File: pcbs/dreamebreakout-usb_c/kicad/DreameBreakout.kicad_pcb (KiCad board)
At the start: 2 copper layers, 18 x 61.5 mm, 10 parts, among them J1 SoC Breakout, J1.1 To Robot SoC, J1.2 To Robot MCU, J2 MCU Breakout, J3 OTG_USB, SW1 SoC_Boot_SEL_BTN

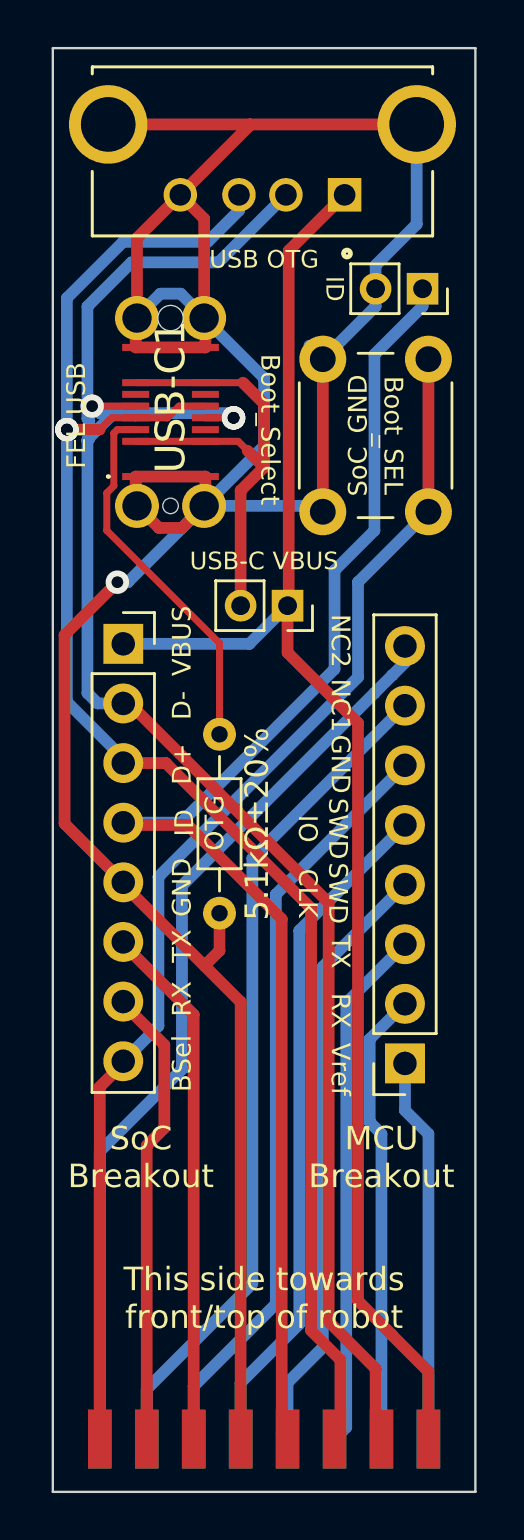
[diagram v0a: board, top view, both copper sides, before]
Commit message: Replaced micro-USB with USB-C receptacle. Also added a second Resistor for symeptric pluggablility
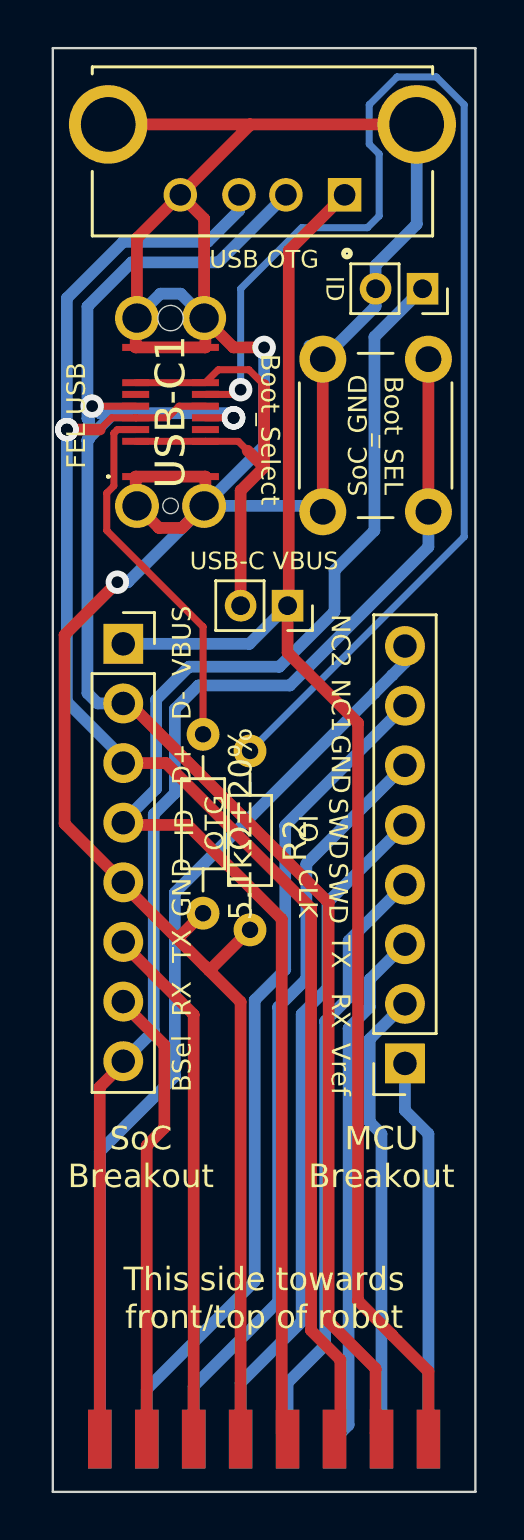
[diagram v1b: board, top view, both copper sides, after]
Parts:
- added R2: 5.1kΩ±20%, Resistor_THT:R_Axial_DIN0204_L3.6mm_D1.6mm_P7.62mm_Horizontal, F.Cu at (58.4, 68.7)
- moved R1 0.70 mm to (56.4, 68.0)
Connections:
- USB-C1 pad B5: unconnected-(USB-C1-CC2-PadB5) -> Net-(USB-C1-CC2)
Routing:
- net Net-(USB-C1-CC2): track 0.00 -> 54.3 mm, vias 0 -> 1
- net SoC_GND: track 131.0 -> 133.3 mm, vias 1 -> 2
- net Boot_SEL: track 51.7 -> 54.0 mm
- net USB_VBUS: track 20.8 -> 21.7 mm
- net SoC_USB_OTG_ID: track 60.1 -> 60.9 mm
